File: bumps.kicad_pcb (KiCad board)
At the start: 2 copper layers, 111.1 x 65.4 mm, 131 parts, among them M1 CONN_1, M2 CONN_1, M3 CONN_1, P1 DIL6, P10 Mot-A, P11 Mot-A, P12 Mot-X, P13 T1, P14 T2, P15 T3, P16 MPower, P17 PWM-2, P18 PWM-1, P19 END-X, P2 DIL6, P20 END-Y, P21 END-Z, P22 Mot-X, P23 Mot-Y, P24 Mot-Y, P25 Mot-Z, P26 Mot-Z, P27 Aux, P29 PWM, P3 Mot-E, P4 Mot-E, P5 DIL6, P6 DIL6, P7 DIL6, P8 P8 Header, P9 P9 Header, Q1 IRLB8743PBF, Q2 IRLB8743PBF, Q3 FDS9926A, Q4 FDS9926A, U1 E-Polo, U2 A-Polo, U3 X-Polo, U4 Y-Polo, U5 Z-Polo, U6 MC34063, U7 AP1117/3.3

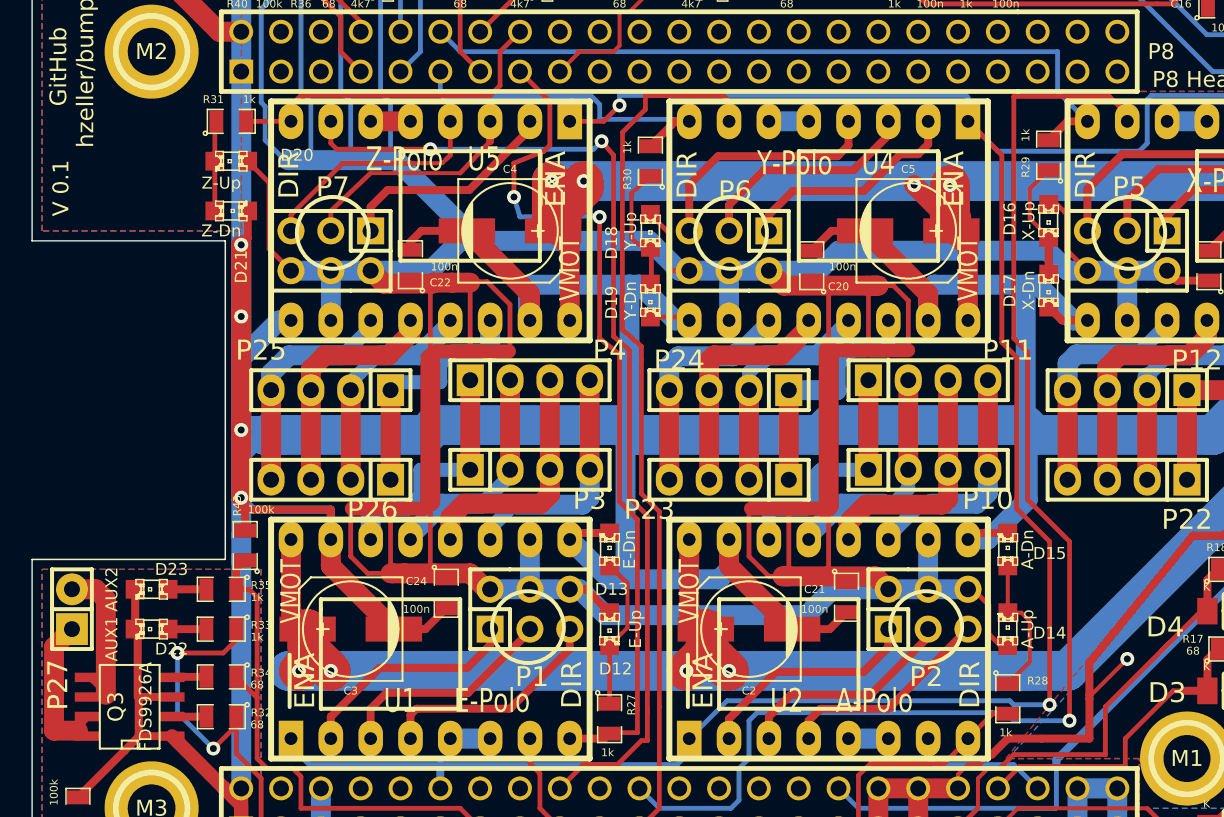
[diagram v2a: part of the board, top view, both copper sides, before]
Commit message: o Add 4k7 pullup to ~Enable o Version number on board-text bumped to v0.2 o Addresses 'enable' part of issue #4
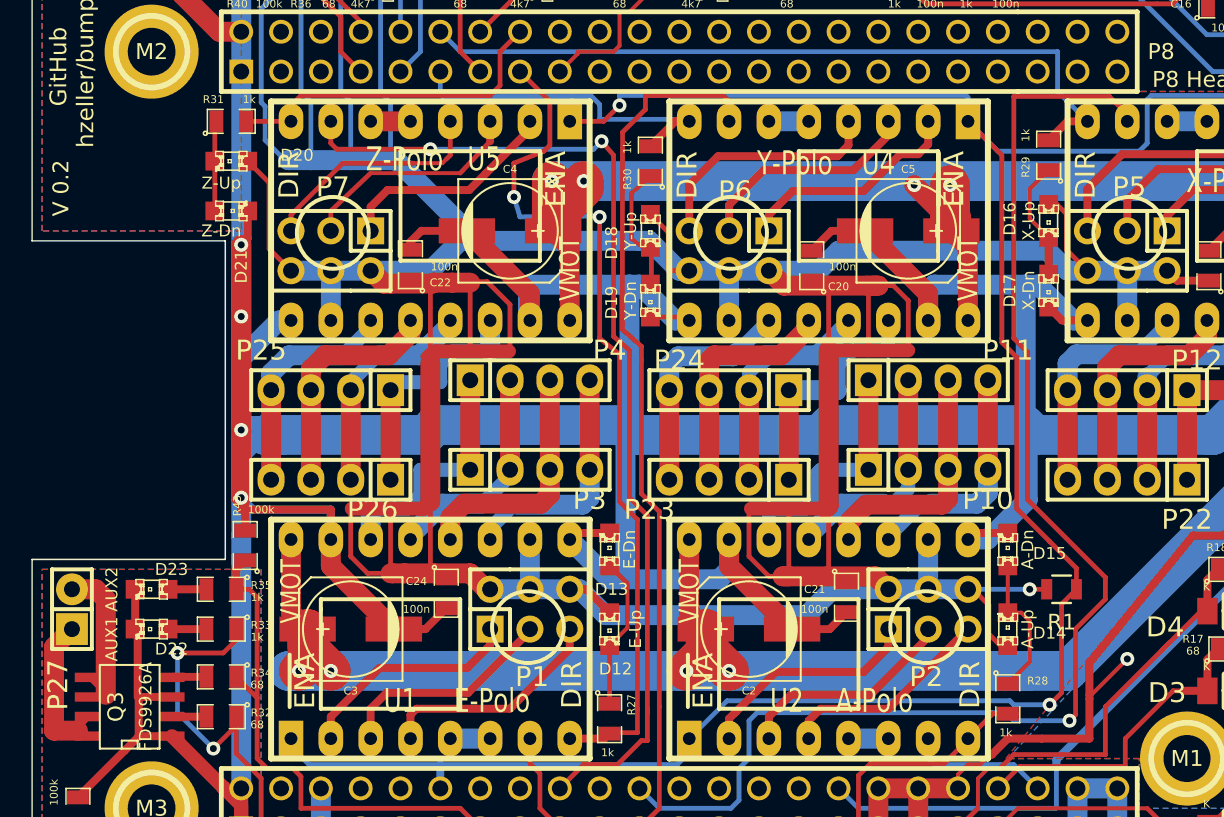
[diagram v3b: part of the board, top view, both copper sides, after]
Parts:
- added R1: 4k7, Resistors_SMD:R_0805, F.Cu at (113.3, 74.9)
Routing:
- net VDD_3V3: track 444.1 -> 449.2 mm, vias 5 -> 6
- net STEP_X: track 82.9 -> 84.8 mm
- net ~EN: track 151.6 -> 153.0 mm
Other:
- board text added: "V 0.2"
- board text removed: "V 0.1"
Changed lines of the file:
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@@
 (kicad_pcb (version 4) (host pcbnew "(2015-02-28 BZR 5464)-product")
   (general
-    (links 322)
+    (links 324)
     (no_connects 0)
     (area 47.574999 27.889999 158.800001 93.395001)
     (thickness 1.6)
     (drawings 30)
-    (tracks 1391)
+    (tracks 1401)
     (zones 0)
-    (modules 131)
+    (modules 132)
     (nets 104)
   )
@@
   )
   (setup
-    (last_trace_width 0.508)
+    (last_trace_width 0.3048)
     (user_trace_width 0.3048)
     (user_trace_width 0.508)
@@
     )
   )
+  (module Resistors_SMD:R_0805 (layer F.Cu)
+    (at 113.284 74.93 180)
+    (descr "Resistor SMD 0805, reflow soldering, Vishay (see dcrcw.pdf)")
+    (tags "resistor 0805")
+    (attr smd)
+    (fp_text reference R1 (at 0 -2.1 180) (layer F.SilkS)
+      (effects (font (size 1 1) (thickness 0.15)))
+    )
+    (fp_text value 4k7 (at 0 2.1 180) (layer F.Fab)
+      (effects (font (size 1 1) (thickness 0.15)))
+    )
+    (fp_line (start -1.6 -1) (end 1.6 -1) (layer F.CrtYd) (width 0.05))
+    (fp_line (start -1.6 1) (end 1.6 1) (layer F.CrtYd) (width 0.05))
+    (fp_line (start -1.6 -1) (end -1.6 1) (layer F.CrtYd) (width 0.05))
+    (fp_line (start 1.6 -1) (end 1.6 1) (layer F.CrtYd) (width 0.05))
+    (fp_line (start 0.6 0.875) (end -0.6 0.875) (layer F.SilkS) (width 0.15))
+    (fp_line (start -0.6 -0.875) (end 0.6 -0.875) (layer F.SilkS) (width 0.15))
+    (pad 1 smd rect (at -0.95 0 180) (size 0.7 1.3) (layers F.Cu F.Paste F.Mask)
+      (net 103 ~EN))
+    (pad 2 smd rect (at 0.95 0 180) (size 0.7 1.3) (layers F.Cu F.Paste F.Mask)
+      (net 99 VDD_3V3))
+    (model Resistors_SMD.3dshapes/R_0805.wrl
+      (at (xyz 0 0 0))
+      (scale (xyz 1 1 1))
+      (rotate (xyz 0 0 0))
+    )
+  )
   (gr_text + (at 156.464 33.02 90) (layer F.SilkS)
     (effects (font (size 3.81 3.81) (thickness 0.9525)))
@@
     (effects (font (size 1.0668 1.0668) (thickness 0.2032)))
   )
-  (gr_text "V 0.1" (at 49.4665 49.3395 90) (layer F.SilkS)
+  (gr_text "V 0.2" (at 49.4665 49.3395 90) (layer F.SilkS)
     (effects (font (size 1.016 1.016) (thickness 0.254)))
   )
@@
   (segment (start 80.01 88.9) (end 81.28 90.17) (width 0.3048) (layer F.Cu) (net 92))
   (segment (start 79.375 84.455) (end 79.375 86.0425) (width 0.3048) (layer F.Cu) (net 92))
+  (segment (start 113.792 83.312) (end 114.173 82.931) (width 0.3048) (layer F.Cu) (net 93))
+  (segment (start 108.712 82.804) (end 109.728 82.804) (width 0.3048) (layer B.Cu) (net 93))
+  (segment (start 111.125 59.817) (end 111.125 69.215) (width 0.3048) (layer F.Cu) (net 93))
+  (segment (start 110.236 58.928) (end 110.236 43.4975) (width 0.3048) (layer F.Cu) (net 93))
+  (segment (start 116.332 43.4975) (end 117.475 44.6405) (width 0.3048) (layer F.Cu) (net 93))
+  (segment (start 116.332 43.4975) (end 110.236 43.4975) (width 0.3048) (layer F.Cu) (net 93))
+  (segment (start 110.236 58.928) (end 111.125 59.817) (width 0.3048) (layer F.Cu) (net 93))
+  (via (at 113.792 83.312) (size 0.889) (layers F.Cu B.Cu) (net 93))
+  (segment (start 110.236 83.312) (end 113.792 83.312) (width 0.3048) (layer B.Cu) (net 93))
+  (segment (start 109.728 82.804) (end 110.236 83.312) (width 0.3048) (layer B.Cu) (net 93))
+  (segment (start 116.078 74.168) (end 111.125 69.215) (width 0.3048) (layer F.Cu) (net 93))
+  (segment (start 116.078 75.565) (end 116.078 74.168) (width 0.3048) (layer F.Cu) (net 93))
+  (segment (start 114.173 77.47) (end 116.078 75.565) (width 0.3048) (layer F.Cu) (net 93))
+  (segment (start 114.173 82.931) (end 114.173 77.47) (width 0.3048) (layer F.Cu) (net 93))
   (segment (start 86.36 87.63) (end 87.63 88.9) (width 0.3048) (layer B.Cu) (net 93))
   (segment (start 93.345 83.312) (end 93.853 82.804) (width 0.3048) (layer B.Cu) (net 93))
@@
   (segment (start 108.712 82.804) (end 108.839 82.804) (width 0.3048) (layer B.Cu) (net 93))
   (segment (start 93.853 82.804) (end 108.712 82.804) (width 0.3048) (layer B.Cu) (net 93))
-  (segment (start 109.728 82.804) (end 110.236 83.312) (width 0.3048) (layer B.Cu) (net 93))
-  (segment (start 110.236 83.312) (end 113.792 83.312) (width 0.3048) (layer B.Cu) (net 93))
-  (via (at 113.792 83.312) (size 0.889) (layers F.Cu B.Cu) (net 93))
-  (segment (start 113.792 83.312) (end 113.792 71.882) (width 0.3048) (layer F.Cu) (net 93))
-  (segment (start 113.792 71.882) (end 111.125 69.215) (width 0.3048) (layer F.Cu) (net 93))
-  (segment (start 110.236 58.928) (end 111.125 59.817) (width 0.3048) (layer F.Cu) (net 93))
   (segment (start 117.475 44.6405) (end 117.475 45.085) (width 0.3048) (layer F.Cu) (net 93))
-  (segment (start 116.332 43.4975) (end 110.236 43.4975) (width 0.3048) (layer F.Cu) (net 93))
-  (segment (start 117.475 44.6405) (end 116.332 43.4975) (width 0.3048) (layer F.Cu) (net 93))
-  (segment (start 110.236 58.928) (end 110.236 43.4975) (width 0.3048) (layer F.Cu) (net 93))
-  (segment (start 111.125 59.817) (end 111.125 69.215) (width 0.3048) (layer F.Cu) (net 93))
-  (segment (start 108.712 82.804) (end 109.728 82.804) (width 0.3048) (layer B.Cu) (net 93))
   (segment (start 86.741 44.323) (end 86.741 43.434) (width 0.3048) (layer F.Cu) (net 94))
   (segment (start 85.267802 57.9755) (end 85.267802 58.343802) (width 0.3048) (layer F.Cu) (net 94))
@@
   (segment (start 116.078 82.677) (end 116.078 82.423) (width 0.3048) (layer F.Cu) (net 98))
   (segment (start 116.078 85.471) (end 116.078 82.677) (width 0.3048) (layer F.Cu) (net 98))
+  (segment (start 112.334 74.93) (end 111.252 74.93) (width 0.3048) (layer F.Cu) (net 99))
+  (segment (start 111.252 74.93) (end 107.315 74.93) (width 0.3048) (layer B.Cu) (net 99))
+  (via (at 111.252 74.93) (size 0.889) (layers F.Cu B.Cu) (net 99))
   (segment (start 88.9 54.61) (end 89.535 54.61) (width 1.27) (layer B.Cu) (net 99))
   (segment (start 86.995 52.705) (end 88.9 54.61) (width 1.27) (layer B.Cu) (net 99))
@@
   (via (at 125.476 68.326) (size 0.889) (layers F.Cu B.Cu) (net 102))
   (segment (start 66.802 80.137) (end 89.027 80.137) (width 2.54) (layer B.Cu) (net 102))
+  (segment (start 114.234 74.93) (end 113.284 75.88) (width 0.3048) (layer F.Cu) (net 103))
+  (segment (start 91.948 82.042) (end 109.982 82.042) (width 0.3048) (layer B.Cu) (net 103))
+  (segment (start 109.982 82.042) (end 110.236 82.296) (width 0.3048) (layer B.Cu) (net 103))
+  (segment (start 110.236 82.296) (end 112.522 82.296) (width 0.3048) (layer B.Cu) (net 103))
+  (via (at 112.522 82.296) (size 0.889) (layers F.Cu B.Cu) (net 103))
+  (segment (start 91.948 82.042) (end 89.535 84.455) (width 0.3048) (layer B.Cu) (net 103))
+  (segment (start 113.284 81.534) (end 112.522 82.296) (width 0.3048) (layer F.Cu) (net 103))
+  (segment (start 113.284 75.88) (end 113.284 81.534) (width 0.3048) (layer F.Cu) (net 103))
+  (segment (start 112.522 71.882) (end 114.234 73.594) (width 0.3048) (layer F.Cu) (net 103))
+  (segment (start 110.4265 69.215) (end 110.4265 69.7865) (width 0.3048) (layer F.Cu) (net 103))
+  (segment (start 109.474 59.182) (end 110.4265 60.1345) (width 0.3048) (layer F.Cu) (net 103))
+  (segment (start 110.4265 60.1345) (end 110.4265 69.215) (width 0.3048) (layer F.Cu) (net 103))
+  (segment (start 107.315 45.085) (end 109.474 47.244) (width 0.3048) (layer F.Cu) (net 103))
+  (segment (start 109.474 47.244) (end 109.474 58.928) (width 0.3048) (layer F.Cu) (net 103))
+  (segment (start 109.474 58.928) (end 109.474 59.182) (width 0.3048) (layer F.Cu) (net 103))
+  (segment (start 112.522 71.882) (end 110.49 69.85) (width 0.3048) (layer F.Cu) (net 103))
+  (segment (start 110.4265 69.7865) (end 110.49 69.85) (width 0.3048) (layer F.Cu) (net 103))
+  (segment (start 114.234 73.594) (end 114.234 74.93) (width 0.3048) (layer F.Cu) (net 103))
   (segment (start 107.315 45.085) (end 107.188 45.212) (width 0.3048) (layer B.Cu) (net 103))
   (segment (start 107.315 43.561) (end 107.315 45.085) (width 0.3048) (layer B.Cu) (net 103))
@@
   (segment (start 118.999 43.434) (end 132.08 43.434) (width 0.3048) (layer B.Cu) (net 103))
   (segment (start 73.66 87.63) (end 73.66 86.106) (width 0.508) (layer B.Cu) (net 103))
-  (segment (start 110.4265 69.7865) (end 110.49 69.85) (width 0.3048) (layer F.Cu) (net 103))
-  (segment (start 91.948 82.042) (end 89.535 84.455) (width 0.3048) (layer B.Cu) (net 103))
-  (segment (start 112.522 71.882) (end 110.49 69.85) (width 0.3048) (layer F.Cu) (net 103))
-  (segment (start 112.522 82.296) (end 112.522 71.882) (width 0.3048) (layer F.Cu) (net 103))
-  (via (at 112.522 82.296) (size 0.889) (layers F.Cu B.Cu) (net 103))
-  (segment (start 110.236 82.296) (end 112.522 82.296) (width 0.3048) (layer B.Cu) (net 103))
-  (segment (start 109.982 82.042) (end 110.236 82.296) (width 0.3048) (layer B.Cu) (net 103))
-  (segment (start 91.948 82.042) (end 109.982 82.042) (width 0.3048) (layer B.Cu) (net 103))
-  (segment (start 109.474 58.928) (end 109.474 59.182) (width 0.3048) (layer F.Cu) (net 103))
-  (segment (start 109.474 47.244) (end 109.474 58.928) (width 0.3048) (layer F.Cu) (net 103))
-  (segment (start 107.315 45.085) (end 109.474 47.244) (width 0.3048) (layer F.Cu) (net 103))
-  (segment (start 110.4265 60.1345) (end 110.4265 69.215) (width 0.3048) (layer F.Cu) (net 103))
-  (segment (start 109.474 59.182) (end 110.4265 60.1345) (width 0.3048) (layer F.Cu) (net 103))
-  (segment (start 110.4265 69.215) (end 110.4265 69.7865) (width 0.3048) (layer F.Cu) (net 103))
   (zone (net 1) (net_name AGND) (layer B.Cu) (hatch edge 0.508)
     (connect_pads (clearance 0.508))

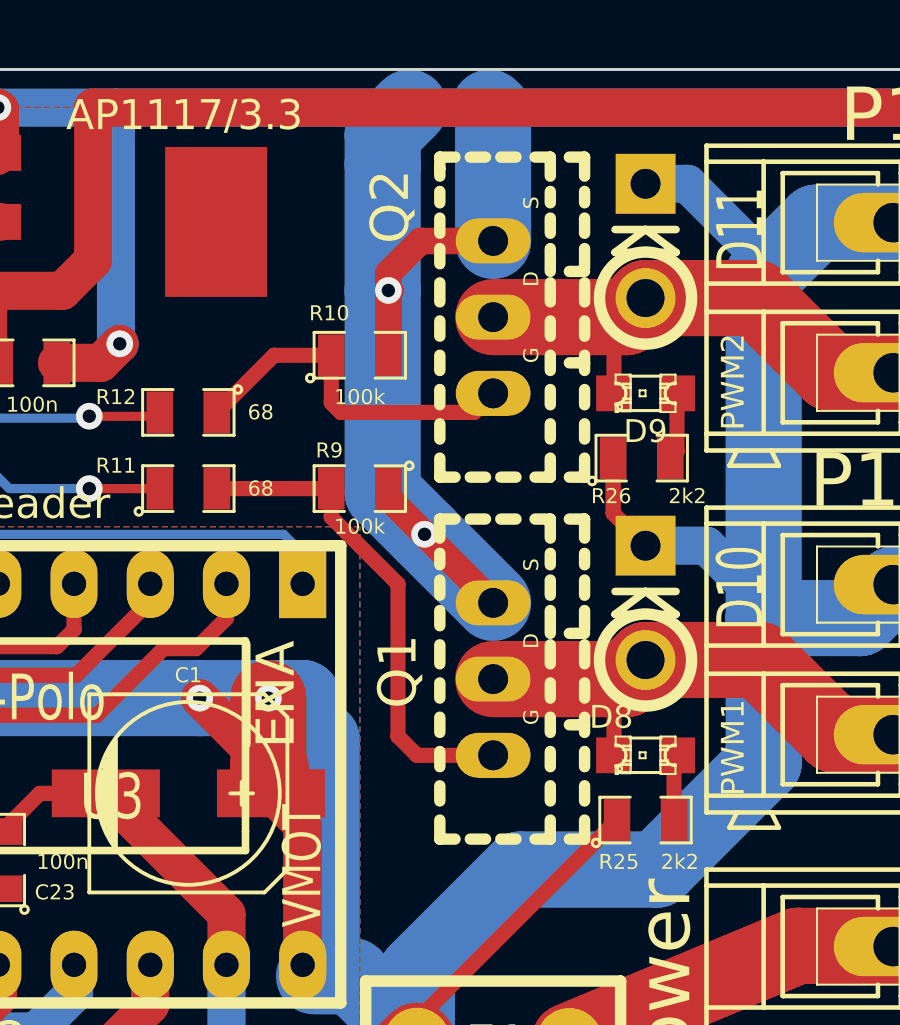
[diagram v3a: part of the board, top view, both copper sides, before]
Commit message: o Change footprint of power-FET to have the heat-sink on the right side. o Addresses part of issue #4
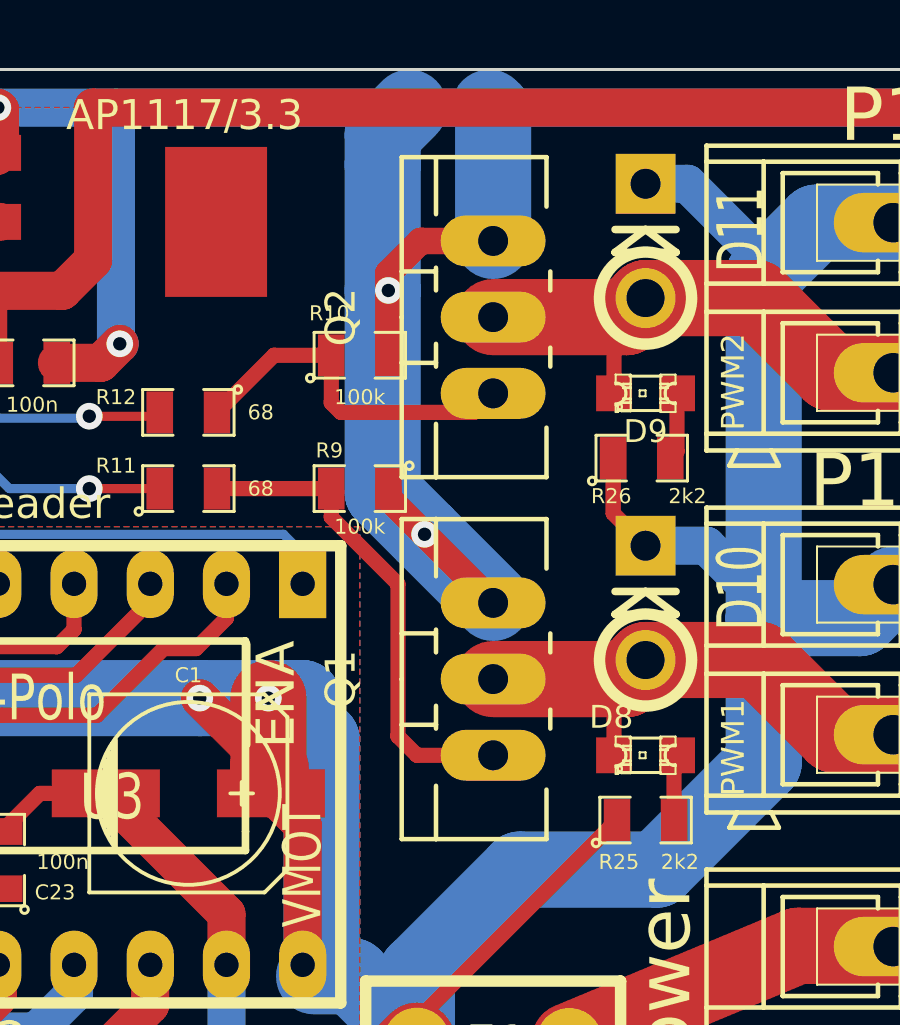
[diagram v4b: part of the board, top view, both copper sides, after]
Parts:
- Q1, Q2: footprint Transistors_TO-220:TO-220_FET-GDS_Vertical_MountedFromLS -> Transistors_TO-220:TO-220_FET-GDS_Vertical_LargePads
- turned Q1 to 90 degrees
- turned Q2 to 90 degrees
